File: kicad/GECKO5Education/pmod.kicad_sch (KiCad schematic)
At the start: 24 parts, among them J3 Conn_02x06_Odd_Even, J4 Conn_02x06_Odd_Even, J6 Conn_01x08_Socket, U13 NCP1529A, U14 NCP1529A, U6 LFE5U-85F-6BG381x, U8 LP5907MFX-2.5, X1 ECS-2520MV-500-BL-TR

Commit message: Small modifications plus added documentation
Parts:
- removed J6: Conn_01x08_Socket, Connector_PinSocket_2.54mm:PinSocket_1x08_P2.54mm_Horizontal, symbol Connector:Conn_01x08_Socket
- added J6: Conn_01x06_Socket, Connector_PinSocket_2.54mm:PinSocket_1x06_P2.54mm_Horizontal, symbol Connector:Conn_01x06_Socket
- added R4: 10k, Resistor_SMD:R_0402_1005Metric, symbol Device:R
- added SW6: B3U-1000P[], gecko4education:SW_B3U-1000P_OMR, symbol gecko5education:B3U-1000P[]
- added X3: CB3LV-3I-74M2500, gecko4education:OSCCC700X500X180-4N, symbol gecko5education:CB3LV-3I-74M2500
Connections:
- net +3.3V: now also J6.1 (Pin_1), R4.1, X3.4 (VCC)
- net GND: now also J6.2 (Pin_2), SW6.2, X3.2 (GND)
- net PMOD3_1: now also J6.6 (Pin_6)
- net PMOD3_2: now also J6.5 (Pin_5)
- net PMOD3_3: now also J6.4 (Pin_4)
- net PMOD3_4: now also J6.3 (Pin_3)
- net USER_CLK1: no longer names the net of U6.G1 (PL47D)
- net USER_CLK1: now also R4.2, SW6.1
- net USER_CLK2: no longer names the net of U6.G2 (PL47A)
- net USER_CLK2: now also X3.3 (OUT)
- no-connect marks 4 -> 5
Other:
- moved on the sheet: SD1

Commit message: Made version V1.5
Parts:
- removed J3: Conn_02x06_Odd_Even, Connector_PinSocket_2.54mm:PinSocket_2x06_P2.54mm_Horizontal, symbol Connector_Generic:Conn_02x06_Odd_Even
- removed SD1: 104031-0811, gecko4education:microsd, symbol gecko5education:micro_sd
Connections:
- net PMOD1_1: no longer U6.P4 (PL92D)
- net PMOD1_10: no longer U6.L3 (PL86C)
- net PMOD1_2: no longer U6.N4 (PL83C)
- net PMOD1_3: no longer U6.M4 (PL83A)
- net PMOD1_4: no longer U6.L4 (PL56C)
- net PMOD1_7: no longer U6.P3 (PL92C)
- net PMOD1_8: no longer U6.N3 (PL86A)
- net PMOD1_9: no longer U6.M3 (PL86B)
- net SD_CLK renamed HDMI_Red4
- net SD_CMD renamed HDMI_Red3
- net SD_D0 renamed HDMI_SCL
- net SD_D1 renamed HDMI_SDA
- net SD_D2 renamed HDMI_Red2
- net SD_D3 renamed HDMI_Blue4
- new net HDMI_Green0: U6.L3 (PL86C)
- new net HDMI_Green1: U6.L4 (PL56C)
- new net HDMI_Green2: U6.M3 (PL86B)
- new net HDMI_Green3: U6.M4 (PL83A)
- new net HDMI_Green4: U6.N3 (PL86A)
- new net HDMI_Green5: U6.N4 (PL83C)
- new net HDMI_Red0: U6.P3 (PL92C)
- new net HDMI_Red1: U6.P4 (PL92D)
- no-connect marks 5 -> 2

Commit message: Made V1.6
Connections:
- net HDMI_Green5 is gone; now on net HDMI_Green0: U6.N4 (PL83C)
- net HDMI_Red0 is gone; now on net HDMI_Green1: U6.P3 (PL92C)
- net HDMI_Red1 is gone; now on net HDMI_Green2: U6.P4 (PL92D)
- net HDMI_SCL is gone; now on net HDMI_Green3: U6.N5 (PL83B)
- net HDMI_SDA is gone; now on net HDMI_Green4: U6.P5 (PL83D)
- net PMOD2_10 is gone; now on net PMOD1_10: J4.6 (Pin_6), U6.L2 (PL86D)
- net PMOD2_7 is gone; now on net PMOD1_7: J4.12 (Pin_12), U6.P1 (PL92A)
- net PMOD2_8 is gone; now on net PMOD1_8: J4.10 (Pin_10), U6.N1 (PL89D)
- net PMOD2_9 is gone; now on net PMOD1_9: J4.8 (Pin_8), U6.M1 (PL89B)
- net PMOD3_1 is gone; now on net PMOD2_1: J6.6 (Pin_6), U6.K2 (PL53A)
- net PMOD3_2 is gone; now on net PMOD2_2: J6.5 (Pin_5), U6.J1 (PL53B)
- net PMOD3_3 is gone; now on net PMOD2_3: J6.4 (Pin_4), U6.H1 (PL53C)
- net PMOD3_4 is gone; now on net PMOD2_4: J6.3 (Pin_3), U6.H2 (PL47C)
- net HDMI_Blue4: now also U6.N3 (PL86A); no longer U6.K4 (PL56A)
- net HDMI_Green0: no longer U6.L3 (PL86C)
- net HDMI_Green1: no longer U6.L4 (PL56C)
- net HDMI_Green2: no longer U6.M3 (PL86B)
- net HDMI_Green3: no longer U6.M4 (PL83A)
- net HDMI_Green4: no longer U6.N3 (PL86A)
- net PMOD1_1: now also J4.11 (Pin_11), U6.P2 (PL92B)
- net PMOD1_2: now also J4.9 (Pin_9), U6.N2 (PL89A)
- net PMOD1_3: now also J4.7 (Pin_7), U6.L1 (PL89C)
- net PMOD1_4: now also J4.5 (Pin_5), U6.K1 (PL53D)
- net PMOD2_1: no longer J4.11 (Pin_11), U6.P2 (PL92B)
- net PMOD2_2: no longer J4.9 (Pin_9), U6.N2 (PL89A)
- net PMOD2_3: no longer J4.7 (Pin_7), U6.L1 (PL89C)
- net PMOD2_4: no longer J4.5 (Pin_5), U6.K1 (PL53D)
- net HDMI_Red2 renamed HDMI_Vsync
- net HDMI_Red3 renamed HDMI_De
- net HDMI_Red4 renamed HDMI_Blue2
- new net HDMI_Blue0: U6.L3 (PL86C)
- new net HDMI_Blue1: U6.L4 (PL56C)
- new net HDMI_Blue3: U6.M4 (PL83A)
- new net HDMI_Clk: U6.M3 (PL86B)
- new net HDMI_Hsync: U6.K4 (PL56A)

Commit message: small progress
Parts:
- X1: value ECS-2520MV-500-BL-TR -> ECS-2520MV-491.52-BL-TR
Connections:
- net CLK_50MHz renamed CLK_49.152MHz
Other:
- moved on the sheet: R4, SW6
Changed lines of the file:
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@@
   (junction (at 194.31 138.43) (diameter 0) (color 0 0 0 0)
   )
-  (junction (at 222.25 58.42) (diameter 0) (color 0 0 0 0)
+  (junction (at 218.44 58.42) (diameter 0) (color 0 0 0 0)
   )
   (junction (at 113.03 20.32) (diameter 0) (color 0 0 0 0)
@@
     (stroke (width 0) (type default))
   )
-  (wire (pts (xy 222.25 58.42) (xy 243.84 58.42))
-    (stroke (width 0) (type default))
-  )
-  (wire (pts (xy 220.98 58.42) (xy 222.25 58.42))
+  (wire (pts (xy 218.44 58.42) (xy 243.84 58.42))
+    (stroke (width 0) (type default))
+  )
+  (wire (pts (xy 217.17 58.42) (xy 218.44 58.42))
     (stroke (width 0) (type default))
   )
@@
     (stroke (width 0) (type default))
   )
-  (wire (pts (xy 222.25 55.88) (xy 222.25 58.42))
+  (wire (pts (xy 218.44 55.88) (xy 218.44 58.42))
     (stroke (width 0) (type default))
   )
@@
     )
   )
-  (global_label "CLK_50MHz" (shape output) (at 76.2 73.66 0) (fields_autoplaced)
+  (global_label "CLK_49.152MHz" (shape output) (at 76.2 73.66 0) (fields_autoplaced)
     (effects (font (size 1.27 1.27)) (justify left))
-    (property "Intersheetrefs" "${INTERSHEET_REFS}" (at 89.8705 73.66 0)
+    (property "Intersheetrefs" "${INTERSHEET_REFS}" (at 94.1832 73.66 0)
       (effects (font (size 1.27 1.27)) (justify left) hide)
     )
@@
     )
   )
-  (global_label "CLK_50MHz" (shape input) (at 240.03 53.34 180) (fields_autoplaced)
-    (effects (font (size 1.27 1.27)) (justify right))
-    (property "Intersheetrefs" "${INTERSHEET_REFS}" (at 226.3595 53.34 0)
+  (global_label "CLK_49.152MHz" (shape input) (at 240.03 53.34 180) (fields_autoplaced)
+    (effects (font (size 1.27 1.27)) (justify right))
+    (property "Intersheetrefs" "${INTERSHEET_REFS}" (at 222.0468 53.34 0)
       (effects (font (size 1.27 1.27)) (justify right) hide)
     )
@@
     )
   )
-  (symbol (lib_id "Device:R") (at 222.25 52.07 0) (unit 1)
+  (symbol (lib_id "Device:R") (at 218.44 52.07 0) (unit 1)
     (in_bom yes) (on_board yes) (dnp no)
-    (property "Reference" "R4" (at 215.9 52.07 0)
-      (effects (font (size 1.27 1.27)) (justify left))
-    )
-    (property "Value" "10k" (at 215.9 54.61 0)
-      (effects (font (size 1.27 1.27)) (justify left))
-    )
-    (property "Footprint" "Resistor_SMD:R_0402_1005Metric" (at 220.472 52.07 90)
-      (effects (font (size 1.27 1.27)) hide)
-    )
-    (property "Datasheet" "~" (at 222.25 52.07 0)
+    (property "Reference" "R4" (at 212.09 52.07 0)
+      (effects (font (size 1.27 1.27)) (justify left))
+    )
+    (property "Value" "10k" (at 212.09 54.61 0)
+      (effects (font (size 1.27 1.27)) (justify left))
+    )
+    (property "Footprint" "Resistor_SMD:R_0402_1005Metric" (at 216.662 52.07 90)
+      (effects (font (size 1.27 1.27)) hide)
+    )
+    (property "Datasheet" "~" (at 218.44 52.07 0)
       (effects (font (size 1.27 1.27)) hide)
     )
@@
       (effects (font (size 1.27 1.27)))
     )
-    (property "Value" "ECS-2520MV-500-BL-TR" (at 81.28 80.01 0)
+    (property "Value" "ECS-2520MV-491.52-BL-TR" (at 81.28 80.01 0)
       (effects (font (size 1.27 1.27)))
     )
@@
     )
   )
-  (symbol (lib_id "power:+3.3V") (at 222.25 48.26 90) (unit 1)
-    (in_bom yes) (on_board yes) (dnp no) (fields_autoplaced)
-    (property "Reference" "#PWR095" (at 226.06 48.26 0)
-      (effects (font (size 1.27 1.27)) hide)
-    )
-    (property "Value" "+3.3V" (at 218.44 48.26 90)
-      (effects (font (size 1.27 1.27)) (justify left))
-    )
-    (property "Footprint" "" (at 222.25 48.26 0)
-      (effects (font (size 1.27 1.27)) hide)
-    )
-    (property "Datasheet" "" (at 222.25 48.26 0)
+  (symbol (lib_id "power:+3.3V") (at 218.44 48.26 90) (unit 1)
+    (in_bom yes) (on_board yes) (dnp no) (fields_autoplaced)
+    (property "Reference" "#PWR095" (at 222.25 48.26 0)
+      (effects (font (size 1.27 1.27)) hide)
+    )
+    (property "Value" "+3.3V" (at 214.63 48.26 90)
+      (effects (font (size 1.27 1.27)) (justify left))
+    )
+    (property "Footprint" "" (at 218.44 48.26 0)
+      (effects (font (size 1.27 1.27)) hide)
+    )
+    (property "Datasheet" "" (at 218.44 48.26 0)
       (effects (font (size 1.27 1.27)) hide)
     )
@@
     )
   )
-  (symbol (lib_id "power:GND") (at 205.74 58.42 0) (unit 1)
-    (in_bom yes) (on_board yes) (dnp no) (fields_autoplaced)
-    (property "Reference" "#PWR093" (at 205.74 64.77 0)
-      (effects (font (size 1.27 1.27)) hide)
-    )
-    (property "Value" "GND" (at 205.74 63.5 0)
-      (effects (font (size 1.27 1.27)))
-    )
-    (property "Footprint" "" (at 205.74 58.42 0)
-      (effects (font (size 1.27 1.27)) hide)
-    )
-    (property "Datasheet" "" (at 205.74 58.42 0)
+  (symbol (lib_id "power:GND") (at 201.93 58.42 0) (unit 1)
+    (in_bom yes) (on_board yes) (dnp no) (fields_autoplaced)
+    (property "Reference" "#PWR093" (at 201.93 64.77 0)
+      (effects (font (size 1.27 1.27)) hide)
+    )
+    (property "Value" "GND" (at 201.93 63.5 0)
+      (effects (font (size 1.27 1.27)))
+    )
+    (property "Footprint" "" (at 201.93 58.42 0)
+      (effects (font (size 1.27 1.27)) hide)
+    )
+    (property "Datasheet" "" (at 201.93 58.42 0)
       (effects (font (size 1.27 1.27)) hide)
     )
@@
     )
   )
-  (symbol (lib_id "gecko5education:B3U-1000P[]") (at 205.74 58.42 0) (unit 1)
+  (symbol (lib_id "gecko5education:B3U-1000P[]") (at 201.93 58.42 0) (unit 1)
     (in_bom yes) (on_board yes) (dnp no)
-    (property "Reference" "SW6" (at 220.98 60.96 0)
+    (property "Reference" "SW6" (at 217.17 60.96 0)
       (effects (font (size 1.524 1.524)))
     )
-    (property "Value" "B3U-1000P[]" (at 217.17 63.5 0)
+    (property "Value" "B3U-1000P[]" (at 213.36 63.5 0)
       (effects (font (size 1.524 1.524)))
     )
-    (property "Footprint" "gecko4education:SW_B3U-1000P_OMR" (at 205.74 58.42 0)
+    (property "Footprint" "gecko4education:SW_B3U-1000P_OMR" (at 201.93 58.42 0)
       (effects (font (size 1.27 1.27) italic) hide)
     )
-    (property "Datasheet" "B3U-1000P[]" (at 205.74 58.42 0)
+    (property "Datasheet" "B3U-1000P[]" (at 201.93 58.42 0)
       (effects (font (size 1.27 1.27) italic) hide)
     )

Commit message: Added SII9022
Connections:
- net HDMI_Blue4 is gone; now on net HDMI_Clk: U6.N3 (PL86A)
- net HDMI_Green3 is gone; now on net HDMI_Blue2: U6.N5 (PL83B)
- net HDMI_Green4 is gone; now on net HDMI_Green2: U6.P5 (PL83D)
- net HDMI_Blue0: now also U6.M4 (PL83A); no longer U6.L3 (PL86C)
- net HDMI_Blue1: now also U6.M3 (PL86B); no longer U6.L4 (PL56C)
- net HDMI_Blue2: no longer U6.L5 (PL56D)
- net HDMI_Blue3: now also U6.N4 (PL83C); no longer U6.M4 (PL83A)
- net HDMI_Clk: no longer U6.M3 (PL86B)
- net HDMI_De: now also U6.L3 (PL86C); no longer U6.K5 (PL56B)
- net HDMI_Green0: now also U6.P3 (PL92C); no longer U6.N4 (PL83C)
- net HDMI_Green1: now also U6.P4 (PL92D); no longer U6.P3 (PL92C)
- net HDMI_Green2: no longer U6.P4 (PL92D)
- net HDMI_Hsync: now also U6.L4 (PL56C); no longer U6.K4 (PL56A)
- net HDMI_Vsync: now also U6.L5 (PL56D); no longer U6.J5 (PL50B)
- new net HDMI_Sck: U6.J5 (PL50B)
- new net HDMI_Sdo: U6.K4 (PL56A)
- new net HDMI_Ws: U6.K5 (PL56B)

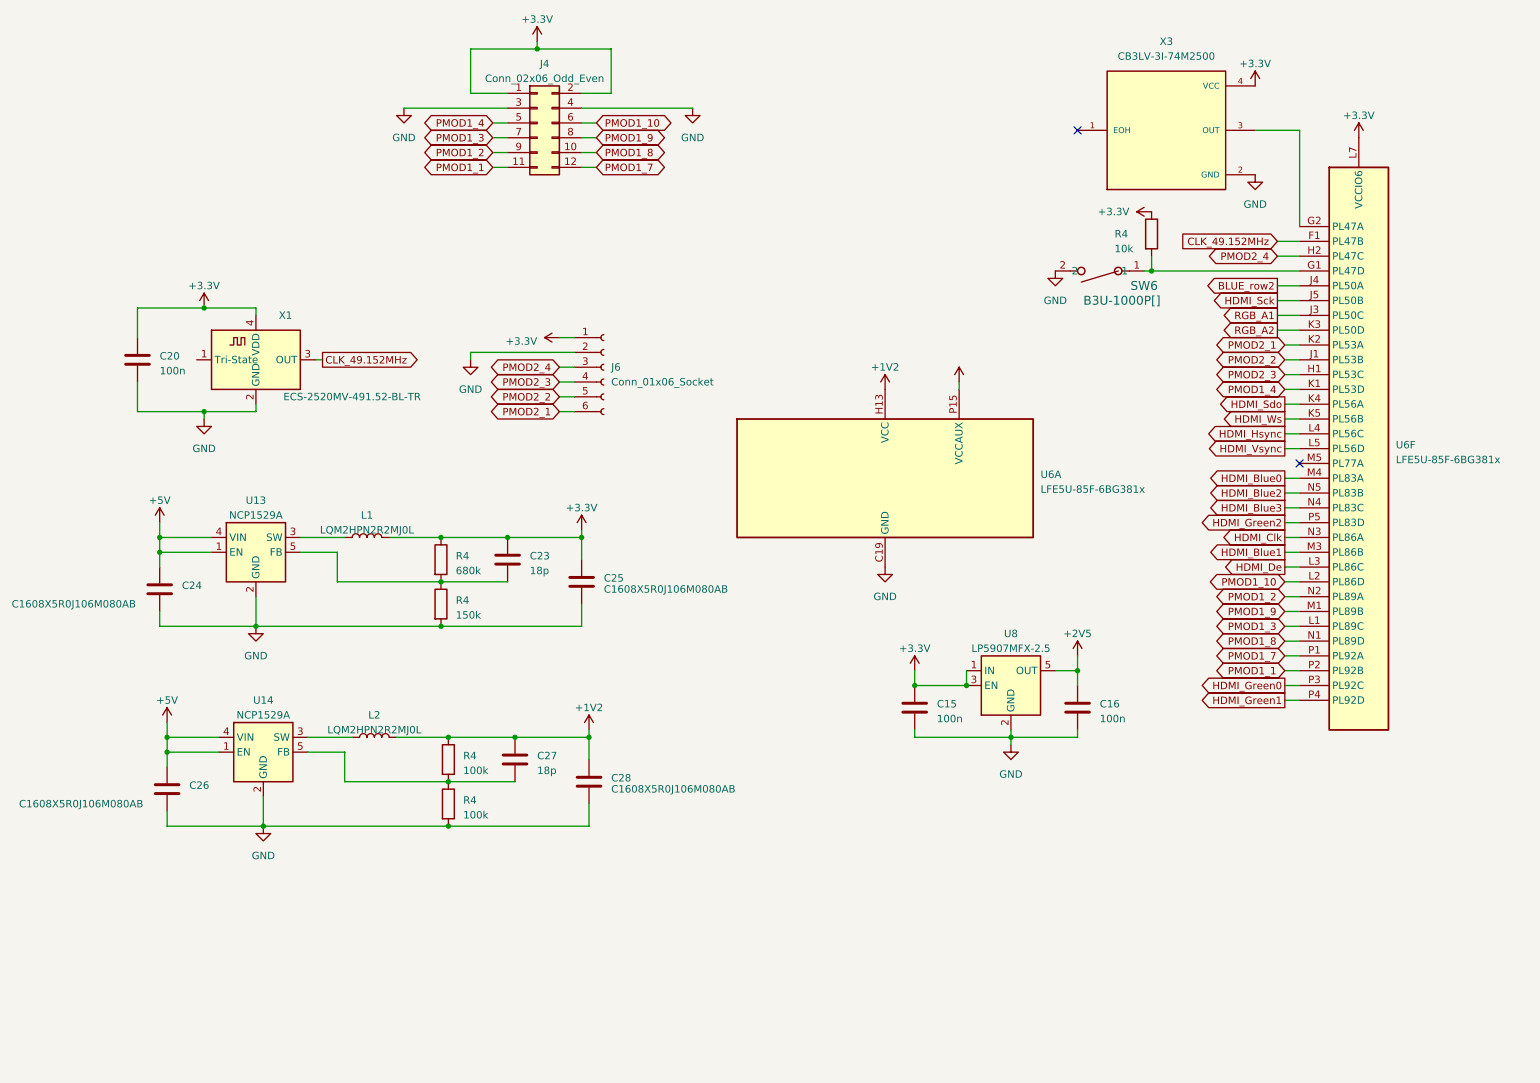
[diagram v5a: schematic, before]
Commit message: Added 2 add-on boards and updated GECKO5 to support olimex camera-OV7670 and an RTC.
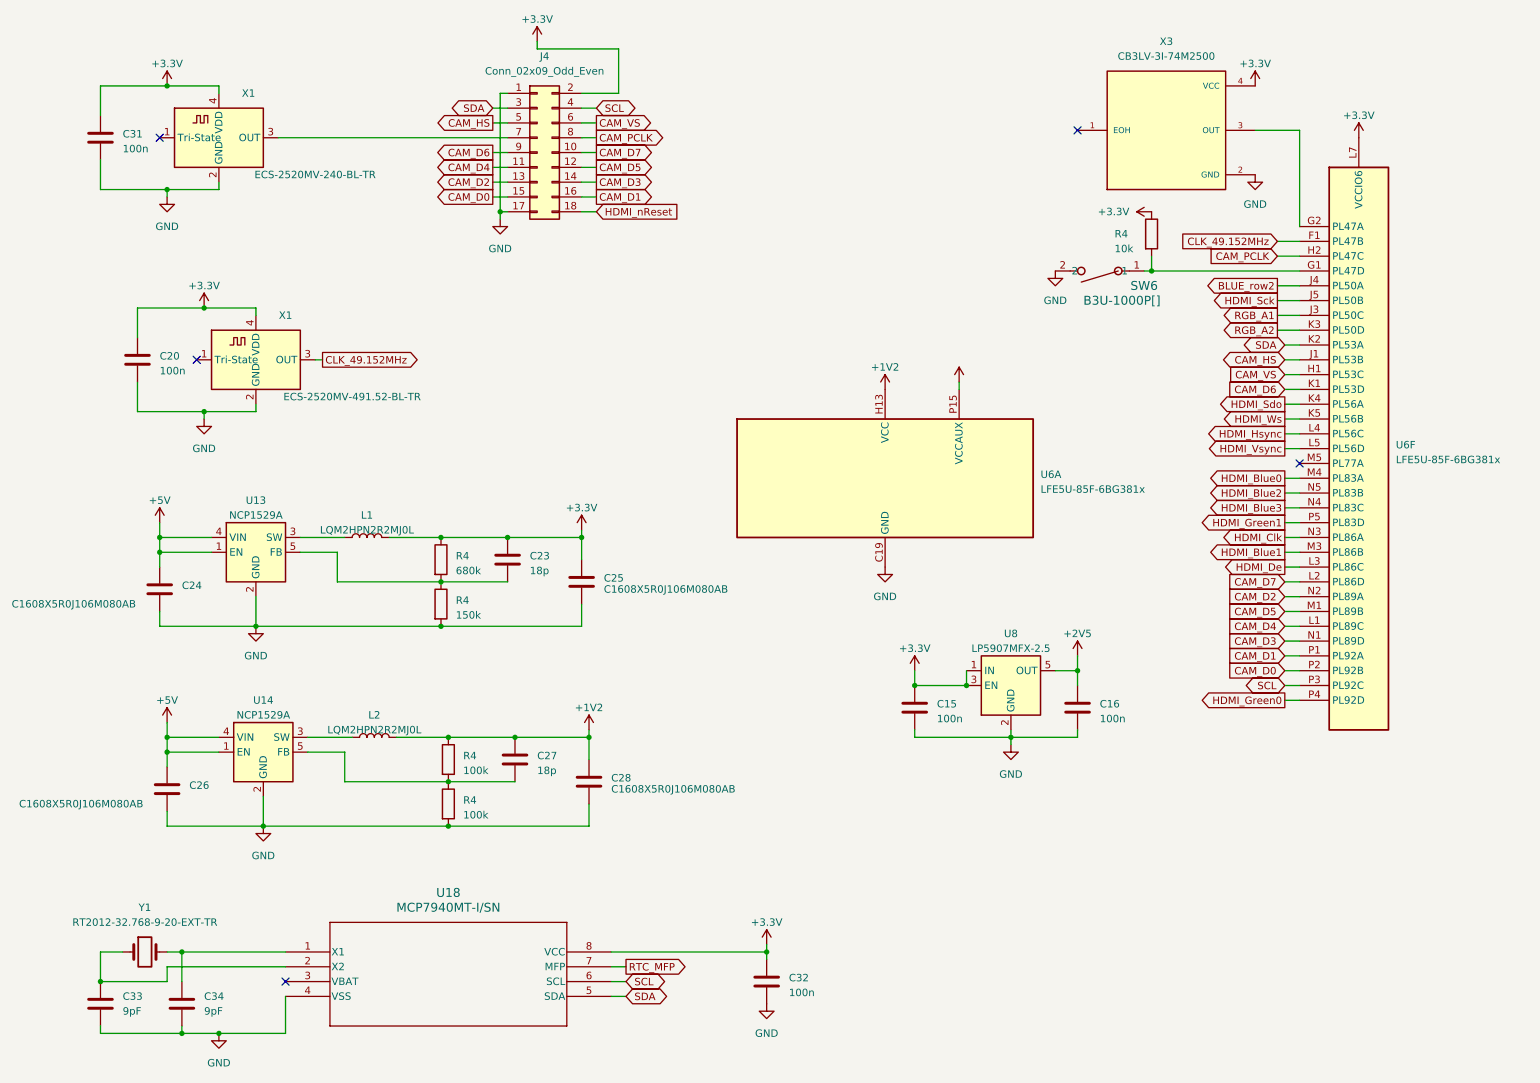
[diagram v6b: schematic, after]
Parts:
- removed J4: Conn_02x06_Odd_Even, Connector_PinSocket_2.54mm:PinSocket_2x06_P2.54mm_Horizontal, symbol Connector_Generic:Conn_02x06_Odd_Even
- removed J6: Conn_01x06_Socket, Connector_PinSocket_2.54mm:PinSocket_1x06_P2.54mm_Horizontal, symbol Connector:Conn_01x06_Socket
- added C31, C32: 100n, Capacitor_SMD:C_0402_1005Metric, symbol Device:C
- added C33, C34: 9pF, Capacitor_SMD:C_0402_1005Metric, symbol Device:C
- added J4: Conn_02x09_Odd_Even, Connector_PinSocket_2.54mm:PinSocket_2x09_P2.54mm_Horizontal, symbol Connector_Generic:Conn_02x09_Odd_Even
- added U18: MCP7940MT-I/SN, gecko4education:SOIC8-N_MC_MCH, symbol gecko5education:MCP7940MT-I_SN
- added X1: ECS-2520MV-240-BL-TR, Oscillator:Oscillator_SMD_ECS_2520MV-xxx-xx-4Pin_2.5x2.0mm, symbol Oscillator:ECS-2520MV-xxx-xx
- added Y1: RT2012-32.768-9-20-EXT-TR, Crystal:Crystal_SMD_2012-2Pin_2.0x1.2mm, symbol Device:Crystal
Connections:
- net HDMI_Green2 is gone; now on net HDMI_Green1: U6.P5 (PL83D)
- net +3.3V: now also C31.1, C32.1, J4.2 (Pin_2), U18.8 (VCC), X1.4 (VDD)
- net GND: now also C31.2, C32.2, C33.2, C34.2, J4.1 (Pin_1), J4.17 (Pin_17), U18.4 (VSS), X1.2 (GND)
- net HDMI_Green0: now also U6.P4 (PL92D); no longer U6.P3 (PL92C)
- net HDMI_Green1: no longer U6.P4 (PL92D)
- net PMOD1_1 renamed CAM_D0
- net CAM_D0: now also J4.15 (Pin_15)
- net PMOD1_10 renamed CAM_D7
- net CAM_D7: now also J4.10 (Pin_10)
- net PMOD1_2 renamed CAM_D2
- net CAM_D2: now also J4.13 (Pin_13)
- net PMOD1_3 renamed CAM_D4
- net CAM_D4: now also J4.11 (Pin_11)
- net PMOD1_4 renamed CAM_D6
- net CAM_D6: now also J4.9 (Pin_9)
- net PMOD1_7 renamed CAM_D1
- net CAM_D1: now also J4.16 (Pin_16)
- net PMOD1_8 renamed CAM_D3
- net CAM_D3: now also J4.14 (Pin_14)
- net PMOD1_9 renamed CAM_D5
- net CAM_D5: now also J4.12 (Pin_12)
- net PMOD2_1 renamed SDA
- net SDA: now also J4.3 (Pin_3), U18.5 (SDA)
- net PMOD2_2 renamed CAM_HS
- net CAM_HS: now also J4.5 (Pin_5)
- net PMOD2_3 renamed CAM_VS
- net CAM_VS: now also J4.6 (Pin_6)
- net PMOD2_4 renamed CAM_PCLK
- net CAM_PCLK: now also J4.8 (Pin_8)
- new net: C33.1, U18.2 (X2), Y1.1
- new net: J4.7 (Pin_7), X1.3 (OUT)
- new net: C34.1, U18.1 (X1), Y1.2
- new net HDMI_nReset: J4.18 (Pin_18)
- new net RTC_MFP: U18.7 (MFP)
- new net SCL: J4.4 (Pin_4), U18.6 (SCL), U6.P3 (PL92C)
- no-connect marks 2 -> 5

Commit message: Final version
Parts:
- X2: renamed from X1; value ECS-2520MV-491.52-BL-TR -> ECS-2520MV-500-BL-TR
- renumbered R4 to R110, R4 to R111, R4 to R112, R4 to R113, R4 to R16, X1 to X4
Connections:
- net HDMI_Sdo is gone; now on net HDMI_Hsync: U6.K4 (PL56A)
- net HDMI_Ws is gone; now on net HDMI_Vsync: U6.K5 (PL56B)
- net HDMI_Blue0: now also U6.L3 (PL86C); no longer U6.M4 (PL83A)
- net HDMI_Blue1: now also U6.M4 (PL83A); no longer U6.M3 (PL86B)
- net HDMI_Blue2: now also U6.M3 (PL86B); no longer U6.N5 (PL83B)
- net HDMI_Blue3: now also U6.N3 (PL86A); no longer U6.N4 (PL83C)
- net HDMI_Clk: now also U6.N4 (PL83C); no longer U6.N3 (PL86A)
- net HDMI_De: now also U6.L4 (PL56C); no longer U6.L3 (PL86C)
- net HDMI_Green0: now also U6.P5 (PL83D); no longer U6.P4 (PL92D)
- net HDMI_Green1: now also U6.N5 (PL83B); no longer U6.P5 (PL83D)
- net HDMI_Hsync: no longer U6.L4 (PL56C)
- net HDMI_Vsync: no longer U6.L5 (PL56D)
- net CLK_49.152MHz renamed CLK_50MHz
- net HDMI_Sck renamed HDMI_Green3
- new net HDMI_Blue4: U6.P4 (PL92D)
- new net HDMI_Green2: U6.L5 (PL56D)
